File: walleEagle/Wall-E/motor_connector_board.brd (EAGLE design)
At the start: 104.1 x 41.9 mm, 32 parts, among them U1 JST_SH_4, U2 JST_SH_6, U3 JST_SH_6, U4 MOLEX_ULTRAFIT, U5 SMC

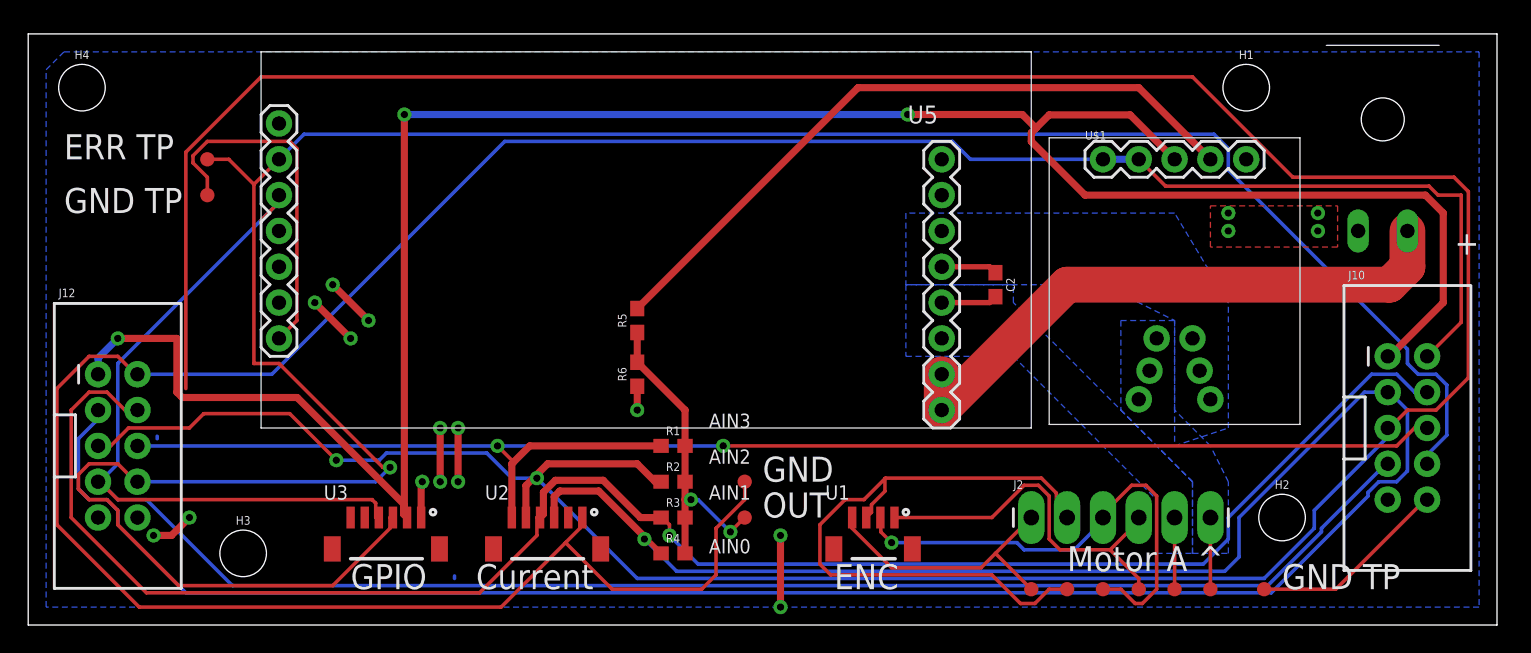
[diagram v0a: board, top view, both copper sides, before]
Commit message: completely redid routing and made standoffs symmetrical
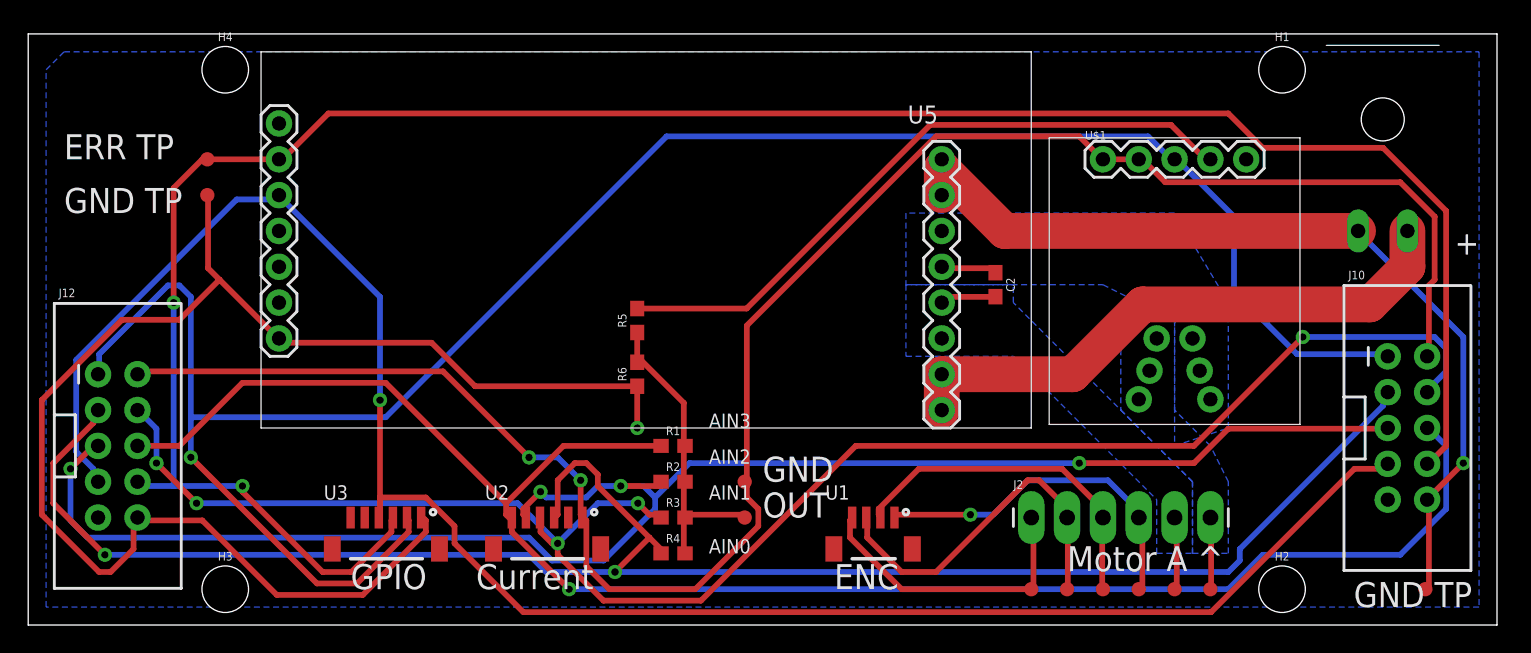
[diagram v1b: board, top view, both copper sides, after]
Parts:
- moved TP2 11.4 mm to (125.7, 0.00)
- moved H4 10.2 mm to (40.6, 36.8)
- moved H2 5.08 mm to (115.6, 0.00)
- moved H3 2.84 mm to (40.6, 0.00)
- moved H1 2.84 mm to (115.6, 36.8)
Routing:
- net AIN2: track 250.1 -> 119.7 mm, vias 2 -> 4
- net GND: track 67.1 -> 166.8 mm, vias 18 -> 2
- net AIN0: track 185.9 -> 128.2 mm, vias 1 -> 2
- net ACS_GND: track 194.2 -> 137.2 mm, vias 0 -> 2
- net SMC_ERR: track 183.2 -> 158.1 mm, vias 1 -> 2
- net ENC_A: track 45.8 -> 26.0 mm
- net ACS_VCC: track 160.9 -> 146.0 mm, vias 3 -> 1
- net AIN3: track 108.5 -> 123.2 mm, vias 2 -> 1
- net SMC_RST: track 147.7 -> 134.4 mm, vias 0 -> 1
- net ENC_VCC: track 34.9 -> 25.0 mm, vias 1 -> 0
- net AIN1: track 126.6 -> 123.6 mm, vias 1 -> 5
- net ACS_3.3OUT: track 49.2 -> 47.0 mm
- net ENC_B: track 19.7 -> 21.1 mm
- net ENC_GND: track 26.7 -> 25.5 mm, vias 0 -> 1
- net VIN: track 42.3 -> 41.3 mm
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- removed copper zone on layer 1, net GND
